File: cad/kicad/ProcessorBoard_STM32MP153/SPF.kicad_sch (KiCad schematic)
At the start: 45 parts, among them J501 SFP, Q501 MMBTA92, Q502 MMBT5551L, Q503 MMBT5551L, Q504 MMBT5551L, Q505 MMBT5551L, Q506 MMBTA92, Q507 MMBT5551L, Q508 MMBTA92, Q509 MMBTA92, U501 DSC6101HL3B-025.0000, U502 TXS0102DCU, X501 RTL8211FS(I)-xx-xx

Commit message: boo womp 10000
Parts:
- removed D501: LED_ABGR, symbol Device:LED_ABGR
- removed Q501, Q506, Q508, Q509: MMBTA92, Package_TO_SOT_SMD:SOT-23, symbol Transistor_BJT:MMBTA92
- removed Q502, Q503, Q504, Q505, Q507: MMBT5551L, Package_TO_SOT_SMD:SOT-23, symbol Transistor_BJT:MMBT5551L
- added C514: 4.7u, Capacitor_SMD:C_0402_1005Metric_Pad0.74x0.62mm_HandSolder, symbol Device:C_Small
- added D503: LED_ABGR, LED_SMD:LED_ASMB-KTF0-0A306, symbol Device:LED_ABGR
- added R515: 330, Resistor_SMD:R_0603_1608Metric_Pad0.98x0.95mm_HandSolder, symbol Device:R_Small_US
- added R516, R517: 240, Capacitor_SMD:C_0402_1005Metric_Pad0.74x0.62mm_HandSolder, symbol Device:R_Small_US
- added R518: 10k, Resistor_SMD:R_0603_1608Metric_Pad0.98x0.95mm_HandSolder, symbol Device:R_Small_US
- added R519: 5.6k, Resistor_SMD:R_0805_2012Metric_Pad1.20x1.40mm_HandSolder, symbol Device:R_Small_US
- added R520: 0, Resistor_SMD:R_0603_1608Metric, symbol Device:R_Small_US
- added U503, U504: SN74LVC07AD, __WM_Local:D0014A_M, symbol __WM_Local:SN84LCV07AD
- C505, U501: now not fitted; now left out of the parts list
- D502: footprint (none) -> LED_SMD:LED_ASMB-KTF0-0A306
- L502, L503: footprint Inductor_SMD:L_1008_2520Metric_Pad1.43x2.20mm_HandSolder -> Inductor_SMD:L_0805_2012Metric_Pad1.05x1.20mm_HandSolder; mouser https://www.mouser.com/en/ProductDetail/Murata-Electronics/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 -> https://www.mouser.com/en/ProductDetail/TDK/MLZ2012M1R0HT00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; unit x1 0.22 -> 0.10; unit x10 0.182 -> 0.079
- R501: value 5.6k -> 100; footprint Resistor_SMD:R_0805_2012Metric_Pad1.20x1.40mm_HandSolder -> Resistor_SMD:R_0402_1005Metric_Pad0.72x0.64mm_HandSolder; mouser https://www.mouser.com/en/ProductDetail/KOA-Speer/RK73H2ATT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 -> https://www.mouser.com/en/ProductDetail/KOA-Speer/RN73R1ETT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; unit x1 0.1 -> 0.10; unit x10 0.021 -> 0.061; unit x100 0.017 -> (none)
- R503: value 330 -> 5.6k; footprint Resistor_SMD:R_0603_1608Metric_Pad0.98x0.95mm_HandSolder -> Resistor_SMD:R_0805_2012Metric_Pad1.20x1.40mm_HandSolder; mouser https://www.mouser.com/en/ProductDetail/Bourns/CR0603-FX-33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 -> https://www.mouser.com/en/ProductDetail/KOA-Speer/RK73H2ATT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; unit x1 0.10 -> 0.1; unit x10 0.012 -> 0.021; unit x100 (none) -> 0.017
- R504: value 240 -> 5.6k; footprint Capacitor_SMD:C_0402_1005Metric_Pad0.74x0.62mm_HandSolder -> Resistor_SMD:R_0805_2012Metric_Pad1.20x1.40mm_HandSolder; mouser https://www.mouser.com/en/ProductDetail/Susumu/RR0510P-241-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 -> https://www.mouser.com/en/ProductDetail/KOA-Speer/RK73H2ATT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; unit x1 0.10 -> 0.1; unit x10 0.023 -> 0.021; unit x100 0.022 -> 0.017
- R505: value 240 -> 2.49k; footprint Capacitor_SMD:C_0402_1005Metric_Pad0.74x0.62mm_HandSolder -> Resistor_SMD:R_0603_1608Metric_Pad0.98x0.95mm_HandSolder; mouser https://www.mouser.com/en/ProductDetail/Susumu/RR0510P-241-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 -> https://www.mouser.com/en/ProductDetail/Susumu/RR0816P-2491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; unit x10 0.023 -> 0.024
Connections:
- net reset is gone; now on an unnamed net: X501.48 (RSET)
- net 3v3: now also R502.2, D503.1 (A), R518.2, U503.14 (VCC); no longer R502.1
- net GND: now also R505.2, C514.1, R519.2, U503.7 (GND), U504.11 (5A), U504.13 (6A), U504.7 (GND); no longer R501.1
- net LED_{1}: now also R519.1, U503.5 (3A); no longer R501.2
- net LED_{2}: now also R502.1, U503.1 (1A); no longer R502.2
- net MOD_PRZ: now also U503.13 (6A)
- net MOD_RX_LOSS: now also U503.11 (5A)
- net MOD_TX_DISABLE: now also U504.8 (4Y)
- net MOD_TX_FAULT: now also U503.9 (4A)
- net V_{io}: now also R503.2, R504.2, X501.29 (DV_{dd}_RG), C514.2, U504.14 (VCC)
- net xtal_out: no longer X501.46 (XTAL_OUT)
- net at R505.1: no longer R503.1
- net sfp.phy.int#: now reaches R504.1
- net sfp.phy.int#: now also X501.34 (INTB/PMEB)
- net at R506.1: now also U504.2 (1Y)
- net at R508.1: now also U504.6 (3Y)
- net at R507.1: now also U504.4 (2Y)
- net at J501.12 (RD-), X501.39 (HS_I_N): now also R501.1
- net at J501.13 (RD+), X501.38 (HS_I_P): now also R501.2
- net sfp.phy.reset#: now reaches X501.13 (PHY_RSTB#)
- net sfp.mdc: now reaches X501.14 (MDC)
- net sfp.mdio: now reaches X501.15 (MDIO)
- net sfp.txd3: now reaches X501.16 (TXD_{3})
- net sfp.txd2: now reaches X501.17 (TXD_{2})
- net sfp.txd1: now reaches X501.18 (TXD_{1})
- net sfp.txd0: now reaches X501.19 (TXD_{0})
- net sfp.txctl: now reaches X501.20 (TXCTL)
- net sfp.txc: now reaches X501.21 (TXCLK)
- net sfp.rxd3: now reaches X501.23 (CFG_{mode2})
- net sfp.rxd2: now reaches X501.24 (CFG_{mode1})
- net sfp.rxd1: now reaches X501.25 (CFG_{mode0})
- net sfp.rxd1: now also R503.1
- net sfp.rxd0: now reaches X501.26 (RXDLY)
- net sfp.rxctl: now reaches X501.27 (PHYAD_{2})
- net sfp.rxc: now reaches X501.28 (PHYAD_{1})
- net at X501.33 (PTP_CLKIN/GPIO_{0}): now also R520.1
- net sfp.phymac_frclk_125: now reaches X501.44 (CLKOUT)
- new net: R515.1, R517.1, U503.4 (2Y)
- new net: D503.2 (BK), R517.2
- new net: R516.1, U503.6 (3Y)
- new net: D503.3 (GK), R516.2
- new net: R518.1, U503.2 (1Y), U503.3 (2A)
- new net: D503.4 (RK), R515.2
- new net sfp.led_{blue}: U504.5 (3A)
- new net sfp.led_{green}: U504.3 (2A)
- new net sfp.led_{red}: U504.1 (1A)
- new net sfp.macphy_clk_25: R520.2, X501.46 (XTAL_OUT)
- new net sfp.module.present: U503.12 (6Y)
- new net sfp.module.rx_loss: U503.10 (5Y)
- new net sfp.module.tx_disable: U504.9 (4A)
- new net sfp.module.tx_fault: U503.8 (4Y)
- no-connect marks 11 -> 13
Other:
- note added: "IO voltage: 1v8 default: 2'b01 set: 2'b10"
- note added: "MDIO addr [2:0] default: 3'b100 set: 3'b100"
- note added: "bridge mode: FIBER <-> RGMII default: 3'b000 set: 3'b001"
- note added: "level shift for processor I2C"
- note added: "see table 55(pg.66) for PTP_CLKIN selection"
- note added: "the RSET resistor isnt in the public datasheet, but NXP reference schematics online show it"
- note removed: "IO voltage 2'b10 : 1v8"
- note removed: "MDIO addr [2:0]"
- note removed: "TODO: figure out the RXD lines D: theyre multi-purpose"
- note removed: "level shift discrete to avoid one off IC's"
- note removed: "level shift for processor"
- note removed: "mode 001: FIBER <-> RGMII"
- moved on the sheet: C501, C502, C503, C504, C506, C507, C508, C509, C510, C511, C512, C513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

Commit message: found reference schematic :he he he ha:
coincidence using the same chip !? am i tweaking or tamale-n brap
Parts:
- removed R504: 5.6k, Resistor_SMD:R_0805_2012Metric_Pad1.20x1.40mm_HandSolder, symbol Device:R_Small_US
- added C515, C516: 4.7u, Capacitor_SMD:C_0402_1005Metric_Pad0.74x0.62mm_HandSolder, symbol Device:C_Small
- added C517: 1n, Capacitor_SMD:C_0402_1005Metric_Pad0.74x0.62mm_HandSolder, symbol Device:C_Small
- added C518, C519: 100n, Capacitor_SMD:C_0402_1005Metric_Pad0.74x0.62mm_HandSolder, symbol Device:C_Small
- J501: Field6 https://www.mouser.com/en/ProductDetail/Amphenol-Commercial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 -> (none); also buy (none) -> https://www.mouser.com/en/ProductDetail/Amphenol-Commercial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
- R501: footprint Resistor_SMD:R_0402_1005Metric_Pad0.72x0.64mm_HandSolder -> Resistor_SMD:R_0402_1005Metric
- R511, R512: now not fitted; now left out of the parts list
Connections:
- net 3v3: now also C501.2, C515.1, C518.2; no longer C501.1
- net GND: now also C501.1, C515.2, C516.2, C517.1, C518.1, C519.1; no longer C501.2, U504.11 (5A)
- net MOD_PRZ: now also U504.11 (5A); no longer U503.13 (6A)
- net V_{io}: now also C516.1, C517.2
- net sfp.module.present: now also U504.10 (5Y); no longer U503.12 (6Y)
- net ir_1v0: now reaches C502.1, C504.1, L501.2, X501.22 (DV_{dd}1v0), X501.4 (AV_{dd}1v0), X501.47 (AV_{dd}1v0), X501.9 (AV_{dd}1v0)
- net ir_1v0: now also C519.2
- net at R517.1, U503.4 (2Y): no longer R515.1
- net ir_out: now reaches L501.1, X501.32 (REG_OUT)
- net SERDES_I_N: now reaches J501.12 (RD-), R501.1, X501.39 (HS_I_N)
- net SERDES_I_P: now reaches J501.13 (RD+), R501.2, X501.38 (HS_I_P)
- net SERDES_O_P: now reaches J501.18 (TD+), X501.40 (HS_O_P)
- net SERDES_O_N: now reaches J501.19 (TD-), X501.41 (HS_O_N)
- net LED_{0}: now reaches X501.35 (PHYAD_{0})
- net LED_{0}: now also U503.13 (6A)
- new net: R515.1, U503.12 (6Y)
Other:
- note added: "* SFP-MSA requires 3v3 I2C lines * internal 10k PU in i2c level shifter IC"
- note added: "MDIO addr [2:0] default: 3'b001 set: 3'b001"
- note added: "MPU I2C level shift"
- note added: "RSET resistor value not in public datasheet, but NXP reference schematics online show it"
- note added: "TODO: interrupt PIN enable internal PU"
- note added: "design from NXP fourm"
- note added: "is this tuff (NF-PR because of quality issues, not trade secrets)"
- note removed: "*SFP-MSA requires 3v3 I2C lines"
- note removed: "MDIO addr [2:0] default: 3'b100 set: 3'b100"
- note removed: "is this tuff"
- note removed: "level shift for processor I2C"
- note removed: "the RSET resistor isnt in the public datasheet, but NXP reference schematics online show it"
- moved on the sheet: C501, C502, C504, C512, C513, C514, D502, D503, J501, L501, R502, R506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

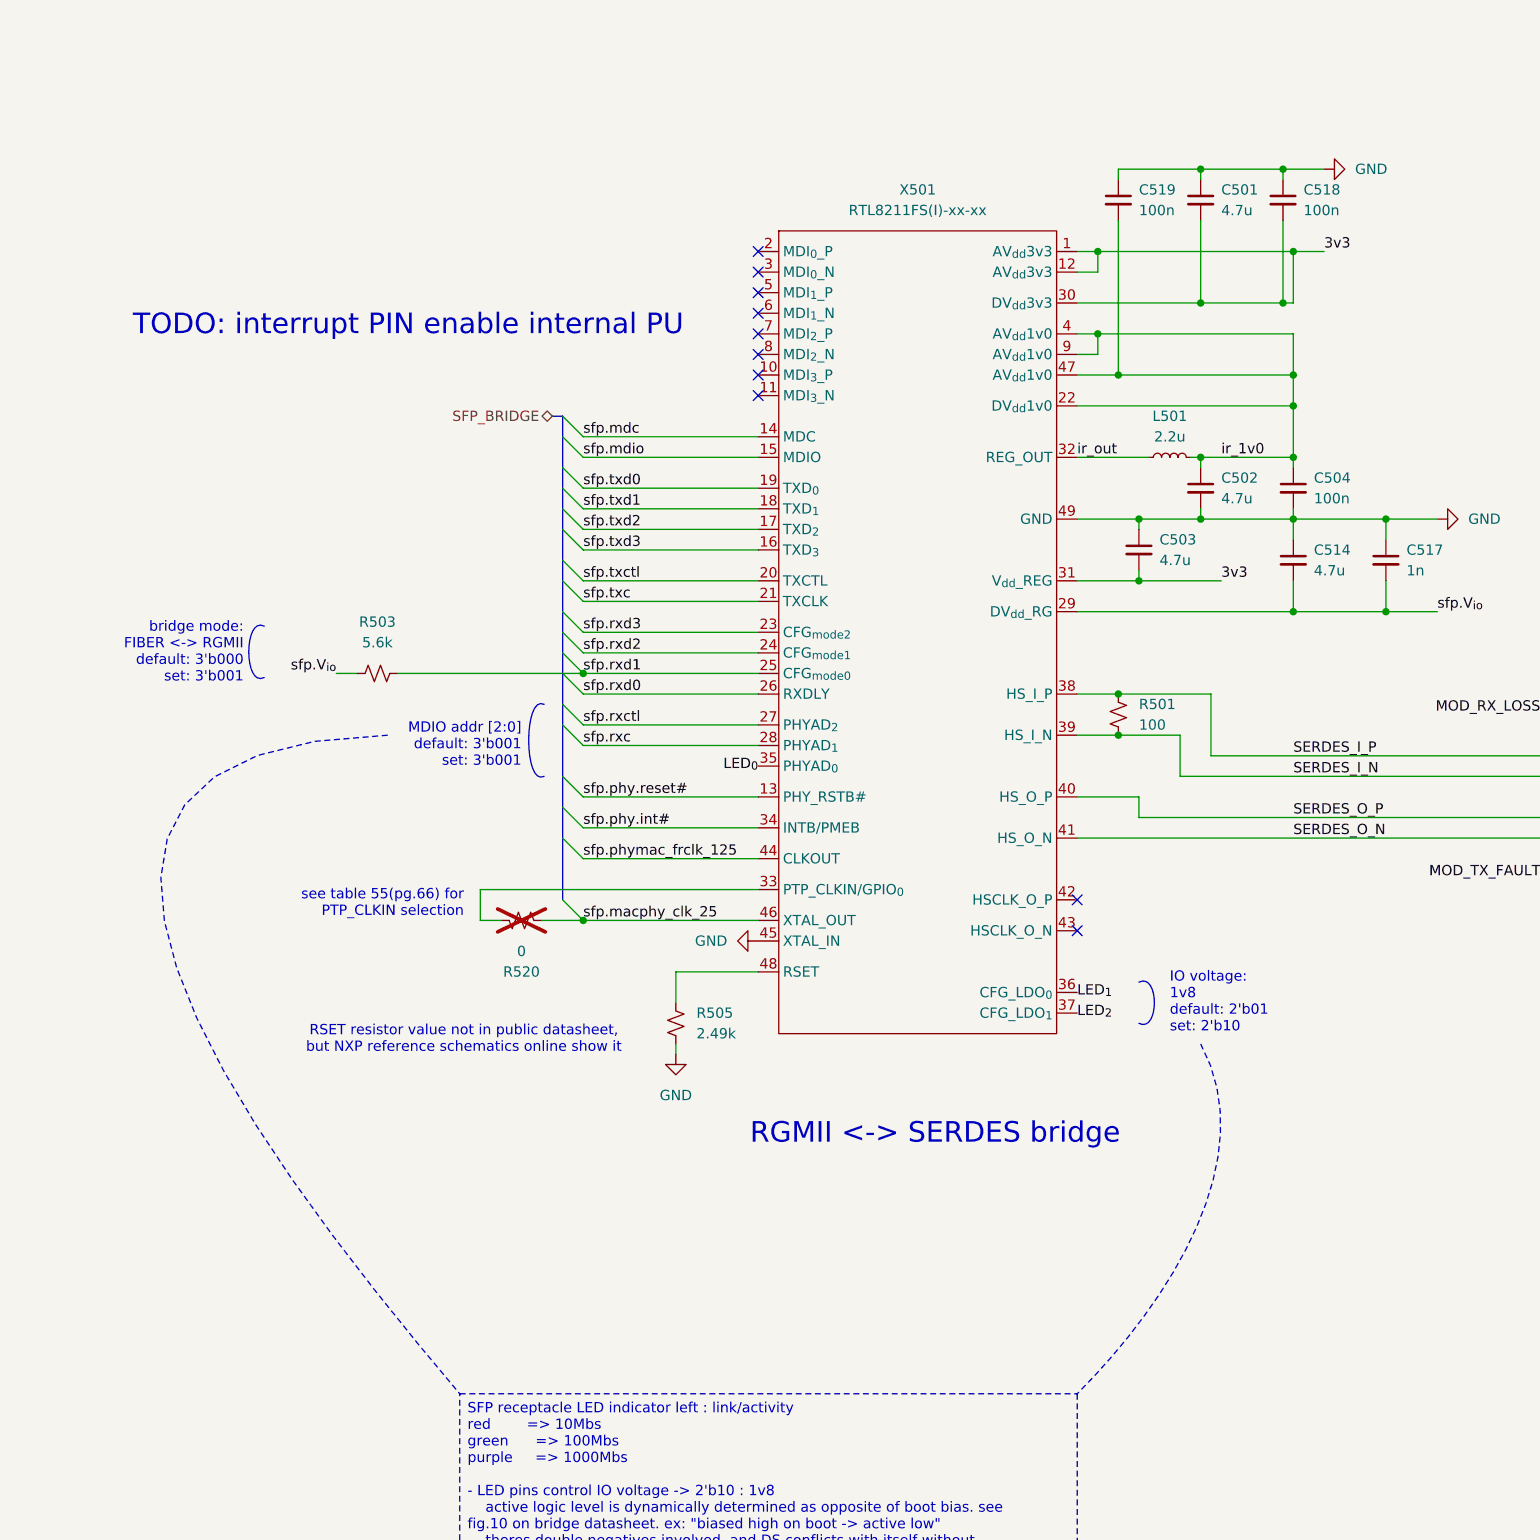
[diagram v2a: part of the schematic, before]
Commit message: i forgor track spacing :(
need to redo ddr
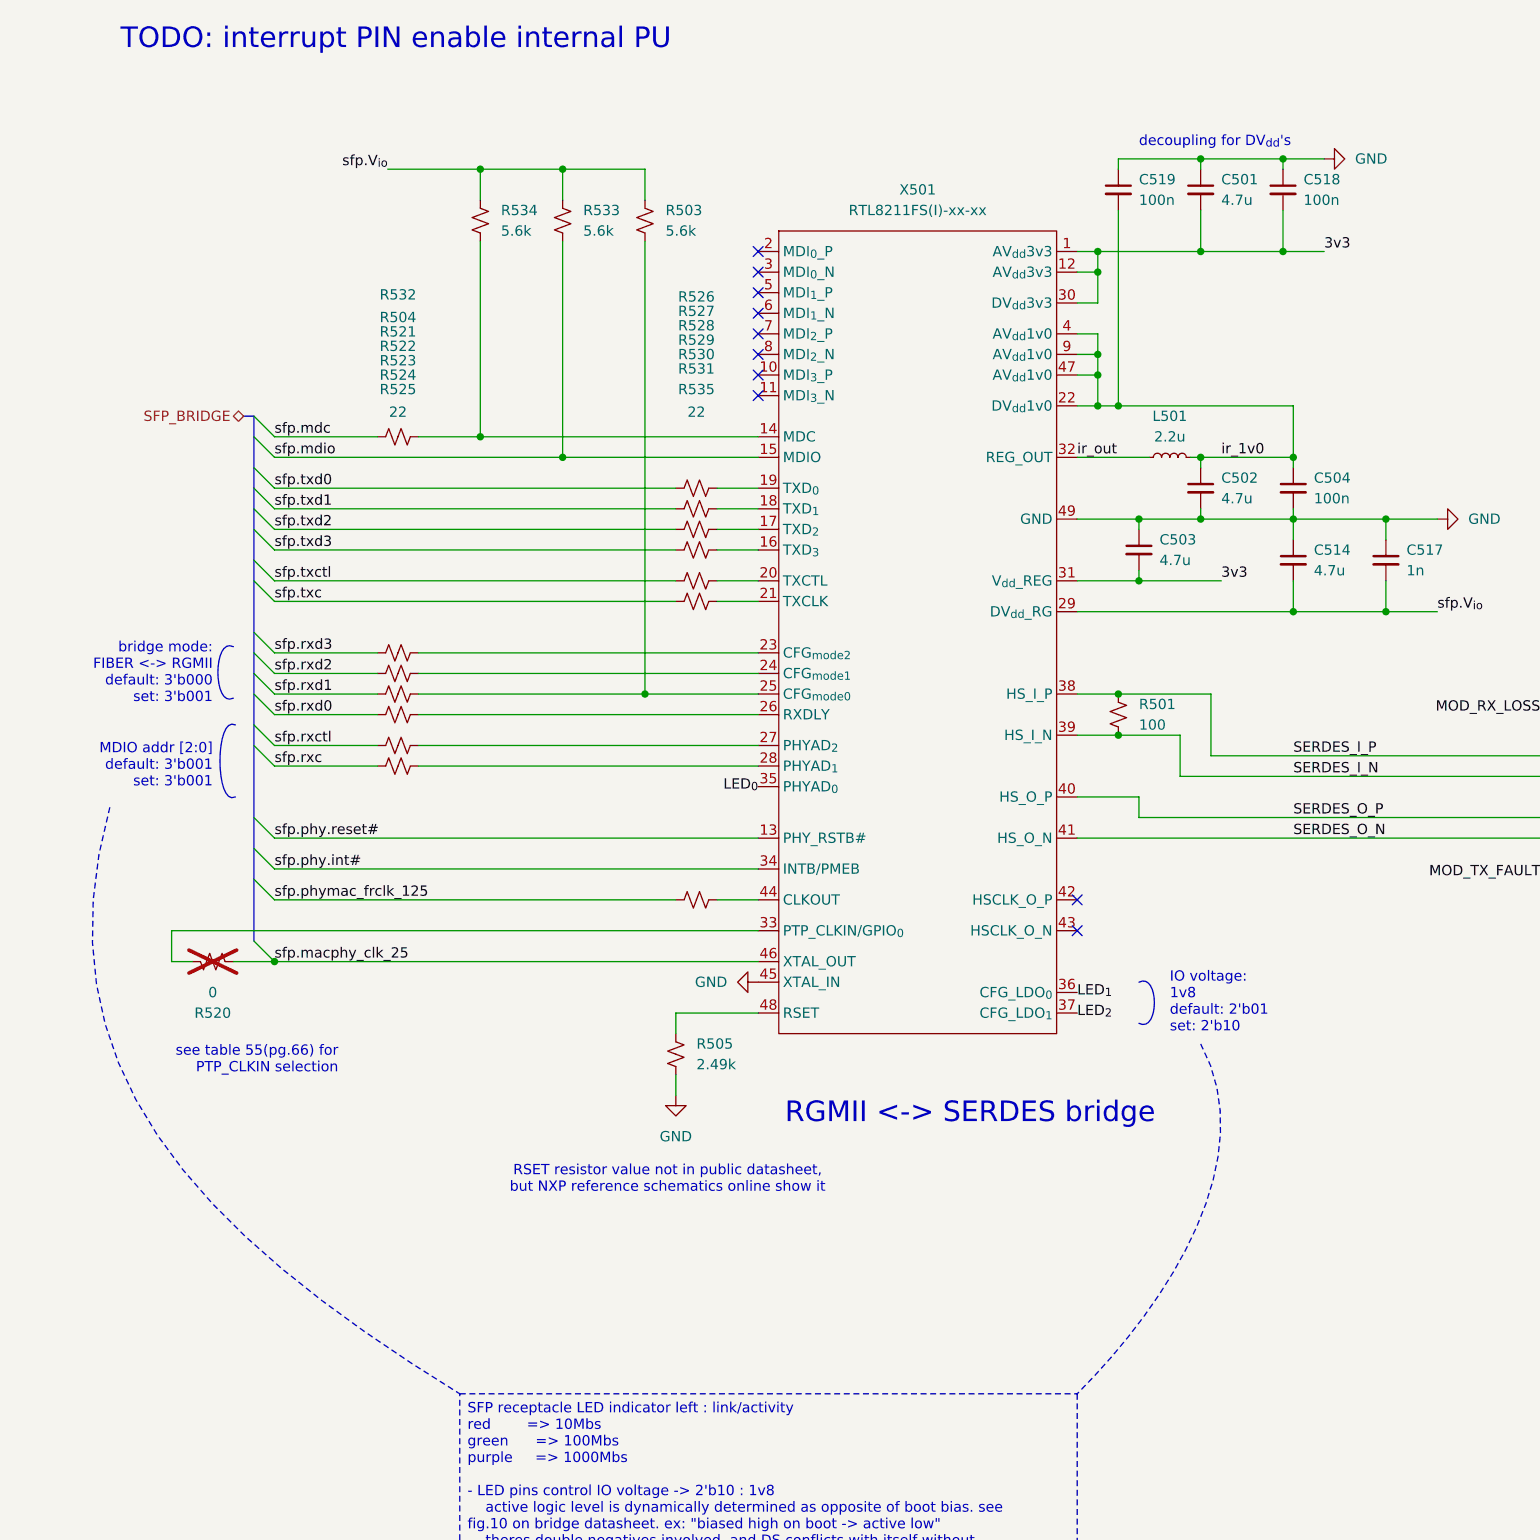
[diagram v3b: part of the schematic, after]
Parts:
- added R504, R521, R522, R523, R524, R525, R526, R527, R528, R529, R530, R531, R532, R535: 22, Resistor_SMD:R_0603_1608Metric, symbol Device:R_Small_US
- added R533, R534: 5.6k, Resistor_SMD:R_0805_2012Metric_Pad1.20x1.40mm_HandSolder, symbol Device:R_Small_US
- added unit 5 of U503
- added unit 1 of U503
- added unit 2 of U503
- added unit 3 of U503
- added unit 7 of U503
- added unit 4 of U503
- added unit 7 of U504
- added unit 5 of U504
- added unit 1 of U504
- added unit 4 of U504
- added unit 3 of U504
- added unit 2 of U504
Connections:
- net 3v3: now also U503.14 (VCC); no longer U503.14 (VCC)
- net GND: now also U503.7 (GND), U504.13 (6A), U504.7 (GND); no longer U503.7 (GND), U504.13 (6A), U504.7 (GND)
- net LED_{0}: now also U503.13 (6A); no longer U503.13 (6A)
- net LED_{1}: now also U503.5 (3A); no longer U503.5 (3A)
- net LED_{2}: now also U503.1 (1A); no longer U503.1 (1A)
- net MOD_TX_DISABLE: now also U504.8 (4Y); no longer U504.8 (4Y)
- net MOD_TX_FAULT: now also U503.9 (4A); no longer U503.9 (4A)
- net V_{io}: now also R503.1, R533.1, R534.1, U504.14 (VCC); no longer R503.2, U504.14 (VCC)
- net sfp.led_{blue}: now also U504.5 (3A); no longer U504.5 (3A)
- net sfp.led_{green}: now also U504.3 (2A); no longer U504.3 (2A)
- net sfp.led_{red}: now also U504.1 (1A); no longer U504.1 (1A)
- net sfp.mdc: now also R532.1; no longer X501.14 (MDC)
- net sfp.mdio: now also R533.2
- net sfp.module.tx_disable: now also U504.9 (4A); no longer U504.9 (4A)
- net sfp.module.tx_fault: now also U503.8 (4Y); no longer U503.8 (4Y)
- net sfp.phymac_frclk_125: now also R535.1; no longer X501.44 (CLKOUT)
- net sfp.rxc: now also R525.1; no longer X501.28 (PHYAD_{1})
- net sfp.rxctl: now also R524.1; no longer X501.27 (PHYAD_{2})
- net sfp.rxd0: now also R523.1; no longer X501.26 (RXDLY)
- net sfp.rxd1: now also R522.1; no longer R503.1, X501.25 (CFG_{mode0})
- net sfp.rxd2: now also R521.1; no longer X501.24 (CFG_{mode1})
- net sfp.rxd3: now also R504.1; no longer X501.23 (CFG_{mode2})
- net sfp.txc: now also R531.1; no longer X501.21 (TXCLK)
- net sfp.txctl: now also R530.1; no longer X501.20 (TXCTL)
- net sfp.txd0: now also R526.1; no longer X501.19 (TXD_{0})
- net sfp.txd1: now also R527.1; no longer X501.18 (TXD_{1})
- net sfp.txd2: now also R528.1; no longer X501.17 (TXD_{2})
- net sfp.txd3: now also R529.1; no longer X501.16 (TXD_{3})
- net at R506.1: now also U504.2 (1Y); no longer U504.2 (1Y)
- net at R508.1: now also U504.6 (3Y); no longer U504.6 (3Y)
- net at R517.1: now also U503.4 (2Y); no longer U503.4 (2Y)
- net at R507.1: now also U504.4 (2Y); no longer U504.4 (2Y)
- net at R516.1: now also U503.6 (3Y); no longer U503.6 (3Y)
- net at R515.1: now also U503.12 (6Y); no longer U503.12 (6Y)
- new net: R529.2, X501.16 (TXD_{3})
- new net: R523.2, X501.26 (RXDLY)
- new net: R524.2, X501.27 (PHYAD_{2})
- new net: R528.2, X501.17 (TXD_{2})
- new net: R530.2, X501.20 (TXCTL)
- new net: R526.2, X501.19 (TXD_{0})
- new net: R525.2, X501.28 (PHYAD_{1})
- new net: R521.2, X501.24 (CFG_{mode1})
- new net: R531.2, X501.21 (TXCLK)
- new net: R532.2, R534.2, X501.14 (MDC)
- new net: R518.1, U503.2 (1Y), U503.3 (2A)
- new net: R504.2, X501.23 (CFG_{mode2})
- new net: R527.2, X501.18 (TXD_{1})
- new net: R535.2, X501.44 (CLKOUT)
- new net: R503.2, R522.2, X501.25 (CFG_{mode0})
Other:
- note added: "decoupling for DV_{dd}'s"
- moved on the sheet: C501, C518, C519, R503, R505, R520
